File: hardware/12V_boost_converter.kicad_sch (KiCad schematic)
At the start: 33 parts, among them Q201 AO3401A, U201 TPS65131RGE, U202 TPS7A39

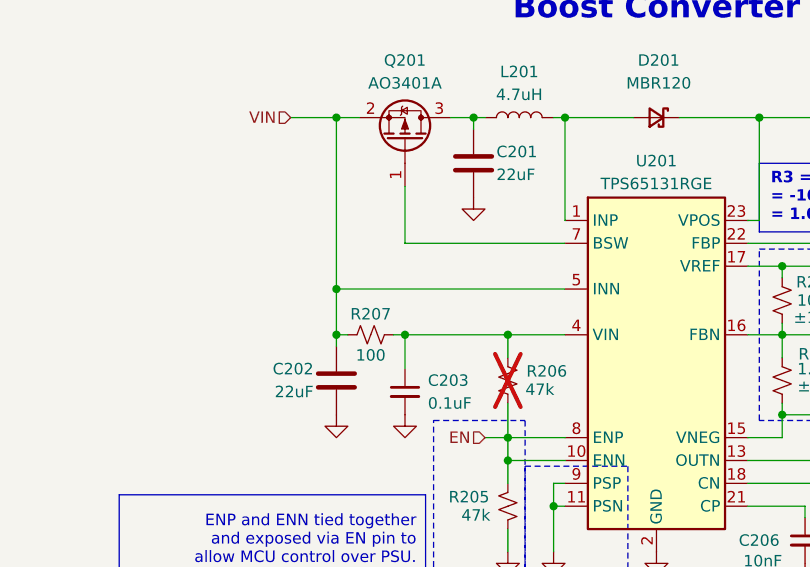
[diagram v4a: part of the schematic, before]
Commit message: Finalize 5V rails
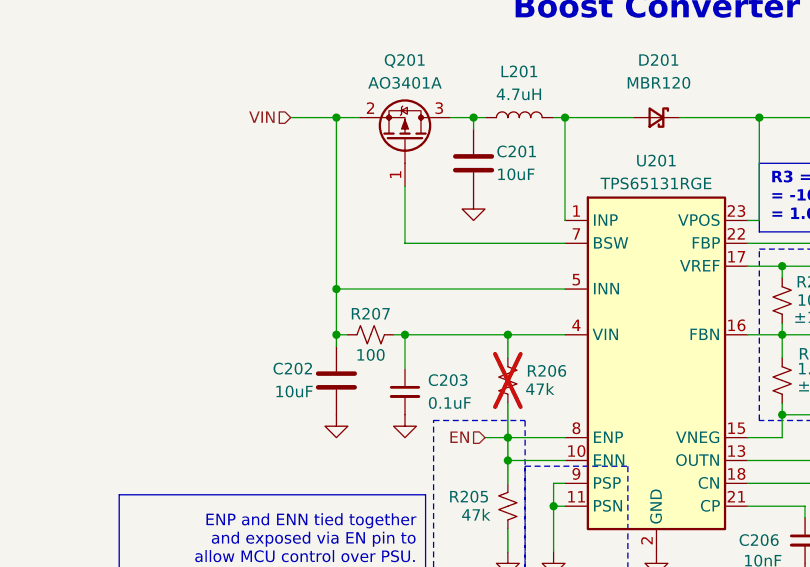
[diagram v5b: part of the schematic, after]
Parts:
- C201, C202: value 22uF -> 10uF
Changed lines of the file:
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@@
 			)
 		)
-		(property "Value" "22uF"
+		(property "Value" "10uF"
 			(at 57.15 93.345 0)
 			(show_name no)
@@
 			)
 		)
-		(property "Value" "22uF"
+		(property "Value" "10uF"
 			(at 77.47 69.215 0)
 			(show_name no)

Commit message: Finalize power
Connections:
- net VIN renamed VBUS_SW
- net VNEG renamed -12VA
- net VPOS renamed +12VA
